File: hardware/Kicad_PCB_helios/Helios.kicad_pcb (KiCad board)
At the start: 2 copper layers, 75.2 x 61.1 mm, 101 parts, among them P1 USB_B, P2 CONN_01X25-SHIELD, U1 IP4220CZ6, U2 AP2114, U3 AN431B, U4 ISA_DC-DC_converter, U5 DAC084S085C, U6 TL084_v, U7 LM358, U8 TL084_v, U9 ATSAM4S, Y1 16MHz 18pF

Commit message: fix some outdated schematics
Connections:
- net /Amplifiers/+9V renamed /+9V
- net /Amplifiers/+B renamed /+B
- net /Amplifiers/+G renamed /+G
- net /Amplifiers/+Intensity renamed /+Int
- net /Amplifiers/+R renamed /+R
- net /Amplifiers/+X renamed /+X
- net /Amplifiers/+Y renamed /+Y
- net /Amplifiers/-9V renamed /-9V
- net /Amplifiers/-X renamed /-X
- net /Amplifiers/-Y renamed /-Y
- net /Amplifiers/2.5V renamed /2.5V
- net /Amplifiers/B renamed /B
- net /Amplifiers/G renamed /G
- net /Amplifiers/Intensity renamed /Int
- net /Amplifiers/R renamed /R
- net /Amplifiers/Shutter renamed /Shutter
- net /Amplifiers/Shutter_Out renamed /Shutter_Out
- net /Amplifiers/X renamed /X
- net /Amplifiers/Y renamed /Y
- net /DAC/!SYNC renamed /!SYNC
- net /DAC/Din renamed /MOSI
- net /DAC/SCLK renamed /SCLK
- net /Power Regulation/5V renamed /VCC
- C10 pad 1: /DAC/3.3V -> /3.3V
- C11 pad 1: /DAC/3.3V -> /3.3V
- C21 pad 1: /DAC/3.3V -> /3.3V
- C23 pad 1: /DAC/3.3V -> /3.3V
- C25 pad 1: /DAC/3.3V -> /3.3V
- C26 pad 1: /DAC/3.3V -> /3.3V
- C27 pad 1: /DAC/3.3V -> /3.3V
- ERASE pad 2: /DAC/3.3V -> (no net)
- R12 pad 1: /DAC/3.3V -> /3.3V
- R13 pad 1: /DAC/3.3V -> /3.3V
- U2 pad 2: /DAC/3.3V -> /3.3V
- U5 pad 1: /DAC/3.3V -> /3.3V
- U9 pad 18: /DAC/3.3V -> /3.3V
- U9 pad 45: /DAC/3.3V -> /3.3V
- U9 pad 58: /DAC/3.3V -> /3.3V
- U9 pad 7: /DAC/3.3V -> /3.3V
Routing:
- net /DAC/3.3V: track 95.3 -> 0.00 mm, vias 2 -> 0
- net /3.3V: track 0.00 -> 95.3 mm, vias 0 -> 2

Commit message: switch to new PSU on PCB. Fix bug in sdk example c++ app
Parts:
- removed REF** (x3): Fiducial_1mm_Dia_2.54mm_Outer_CopperTop, Fiducials:Fiducial_1mm_Dia_2.54mm_Outer_CopperTop
- added H1: MountingHole, MountingHole:MountingHole_2.7mm_M2.5, F.Cu at (161.0, 104.4)
- added H2: MountingHole, MountingHole:MountingHole_2.7mm_M2.5, F.Cu at (104.0, 156.4)
- added H3: MountingHole, MountingHole:MountingHole_2.7mm_M2.5, F.Cu at (104.0, 104.4)
- added H4: MountingHole, MountingHole:MountingHole_2.7mm_M2.5, F.Cu at (161.0, 156.4)
- U4: value ISA_DC-DC_converter -> ~; footprint personal:10-SMD-6 -> personal:CRV1DxxxxSC
- moved U4 11.5 mm to (128.7, 108.4), turned to 0 degrees
- moved C9 5.91 mm to (130.9, 117.8)
- moved C8 4.78 mm to (139.1, 117.8), turned to 180 degrees
- moved F1 0.35 mm to (112.2, 120.3)
- moved C3 0.20 mm to (114.7, 113.5)
- renumbered ERASE to ERASE1
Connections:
- C7 pad 1: Net-(C7-Pad1) -> Net-(U4-Vin)
- D1 pad 2: Net-(D1-Pad2) -> (no net)
- D2 pad 2: Net-(D2-Pad2) -> (no net)
- ERASE1 pad 2: (no net) -> /3.3V
- L2 pad 2: Net-(C7-Pad1) -> Net-(U4-Vin)
- P2 pad 12: (no net) -> /ProjReturn
- R14 pad 2: Net-(R14-Pad2) -> (no net)
- R15 pad 1: Net-(R14-Pad2) -> (no net)
- R16 pad 1: Net-(R16-Pad1) -> (no net)
- R17 pad 1: Net-(R17-Pad1) -> (no net)
- R18 pad 1: Net-(R18-Pad1) -> (no net)
- R19 pad 1: Net-(R19-Pad1) -> (no net)
- R20 pad 2: Net-(R18-Pad1) -> (no net)
- R21 pad 2: Net-(R19-Pad1) -> (no net)
- R22 pad 1: Net-(R22-Pad1) -> (no net)
- R24 pad 1: Net-(R24-Pad1) -> (no net)
- R25 pad 1: Net-(R25-Pad1) -> (no net)
- R26 pad 1: Net-(R26-Pad1) -> (no net)
- R27 pad 1: Net-(R27-Pad1) -> (no net)
- R28 pad 2: Net-(R26-Pad1) -> (no net)
- R29 pad 2: Net-(R27-Pad1) -> (no net)
- R30 pad 1: Net-(R30-Pad1) -> (no net)
- R31 pad 2: Net-(R31-Pad2) -> (no net)
- R32 pad 2: Net-(R31-Pad2) -> (no net)
- R33 pad 1: Net-(R33-Pad1) -> (no net)
- R34 pad 1: Net-(R34-Pad1) -> (no net)
- R35 pad 1: Net-(R35-Pad1) -> (no net)
- R36 pad 1: Net-(R36-Pad1) -> (no net)
- R37 pad 2: Net-(R35-Pad1) -> (no net)
- R38 pad 2: Net-(R36-Pad1) -> (no net)
- R39 pad 1: Net-(R39-Pad1) -> (no net)
- R40 pad 1: Net-(R40-Pad1) -> (no net)
- R41 pad 1: Net-(R41-Pad1) -> (no net)
- R42 pad 1: Net-(R42-Pad1) -> (no net)
- R43 pad 2: Net-(R39-Pad1) -> (no net)
- R44 pad 2: Net-(R40-Pad1) -> (no net)
- R45 pad 2: Net-(D1-Pad2) -> (no net)
- R46 pad 2: Net-(D1-Pad2) -> (no net)
- R47 pad 2: Net-(D2-Pad2) -> (no net)
- R48 pad 2: Net-(D2-Pad2) -> (no net)
- U1 pad 4: (no net) -> unconnected-(U1-IO3-Pad4)
- U1 pad 6: (no net) -> unconnected-(U1-IO4-Pad6)
- U4 pad 1: GND -> Net-(U4-Vin)
- U4 pad 2: Net-(C7-Pad1) -> GND
- U5 pad 8: /MOSI -> /DAC/Din
- U6 pad 10: Net-(R24-Pad1) -> (no net)
- U6 pad 12: Net-(R16-Pad1) -> (no net)
- U6 pad 13: Net-(R18-Pad1) -> (no net)
- U6 pad 2: Net-(R26-Pad1) -> (no net)
- U6 pad 3: Net-(R25-Pad1) -> (no net)
- U6 pad 5: Net-(R17-Pad1) -> (no net)
- U6 pad 6: Net-(R19-Pad1) -> (no net)
- U6 pad 9: Net-(R27-Pad1) -> (no net)
- U7 pad 1: Net-(R22-Pad1) -> (no net)
- U7 pad 2: Net-(R22-Pad1) -> (no net)
- U7 pad 3: Net-(R14-Pad2) -> (no net)
- U7 pad 5: Net-(R30-Pad1) -> (no net)
- U7 pad 6: Net-(R31-Pad2) -> (no net)
- U8 pad 10: Net-(R34-Pad1) -> (no net)
- U8 pad 12: Net-(R41-Pad1) -> (no net)
- U8 pad 13: Net-(R39-Pad1) -> (no net)
- U8 pad 2: Net-(R36-Pad1) -> (no net)
- U8 pad 3: Net-(R33-Pad1) -> (no net)
- U8 pad 5: Net-(R42-Pad1) -> (no net)
- U8 pad 6: Net-(R40-Pad1) -> (no net)
- U8 pad 9: Net-(R35-Pad1) -> (no net)
- U9 pad 39: (no net) -> /Microcontroller/NRST
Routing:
- net (no net): track 0.00 -> 141.3 mm, vias 0 -> 4
- net Net-(D1-Pad2): track 35.7 -> 0.00 mm
- net /+9V: track 67.6 -> 77.5 mm
- net Net-(D2-Pad2): track 9.74 -> 0.00 mm
- net GND: track 138.7 -> 129.4 mm
- net Net-(R35-Pad1): track 8.83 -> 0.00 mm
- net Net-(R39-Pad1): track 8.41 -> 0.00 mm, vias 2 -> 0
- net Net-(U4-Vin): track 0.00 -> 6.81 mm
- net /-9V: track 73.0 -> 66.4 mm
- net Net-(C7-Pad1): track 6.53 -> 0.00 mm
- net Net-(R24-Pad1): track 6.38 -> 0.00 mm
- net Net-(R17-Pad1): track 6.33 -> 0.00 mm
- net Net-(R34-Pad1): track 6.09 -> 0.00 mm
- net Net-(R18-Pad1): track 5.17 -> 0.00 mm, vias 2 -> 0
- net Net-(R40-Pad1): track 5.10 -> 0.00 mm
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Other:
- net class Default removed
- board text added: "Gitle Mikkelsen www.bitlasers.com gitlem@gmail.com"
- board text added: "Helios Laser DAC Rev 1.2"
- board text removed: "Gitle Mikkelsen Thomas L Heggland Bård Gustav Hole Eide"
- board text removed: "Helios Laser DAC Rev 1.1"
- board text removed: "gitlem@gmail.com"

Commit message: PCB 1.2
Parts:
- L1, L2, L3, R1, R10, R11, R12, R13, R14, R15, R16, R17, R18, R19, R2, R20, R21, R22, R23, R24, R25, R26, R27, R28, R29, R3, R30, R31, R32, R33, R34, R35, R36, R37, R38, R39, R4, R40, R41, R42, R43, R44, R45, R46, R47, R48, R5, R6, R7, R8, R9: footprint Resistors_SMD:R_0603 -> Resistor_SMD:R_0603_1608Metric
- moved Y1 0.18 mm to (115.7, 145.0)
- turned D1 to 90 degrees
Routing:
- net (no net): track 141.3 -> 143.0 mm

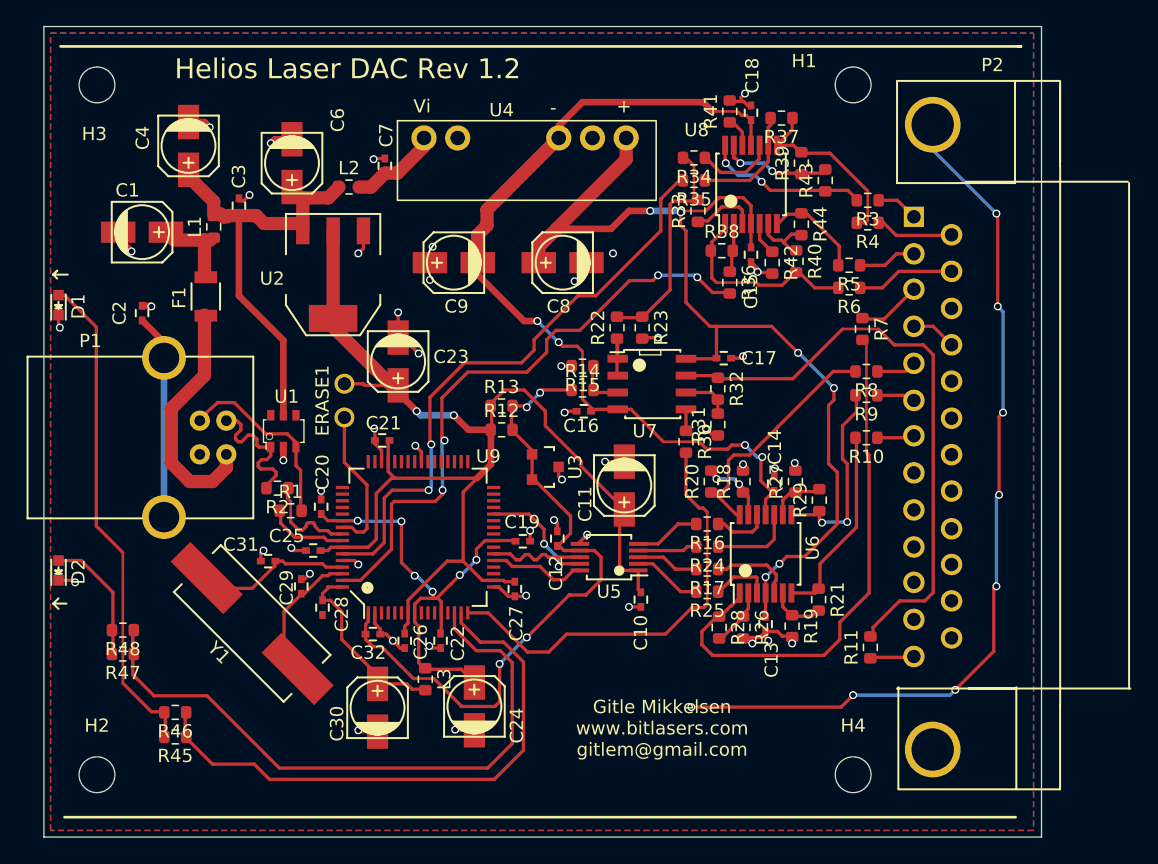
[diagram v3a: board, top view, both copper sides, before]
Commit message: Fix bug with D1 in pcb
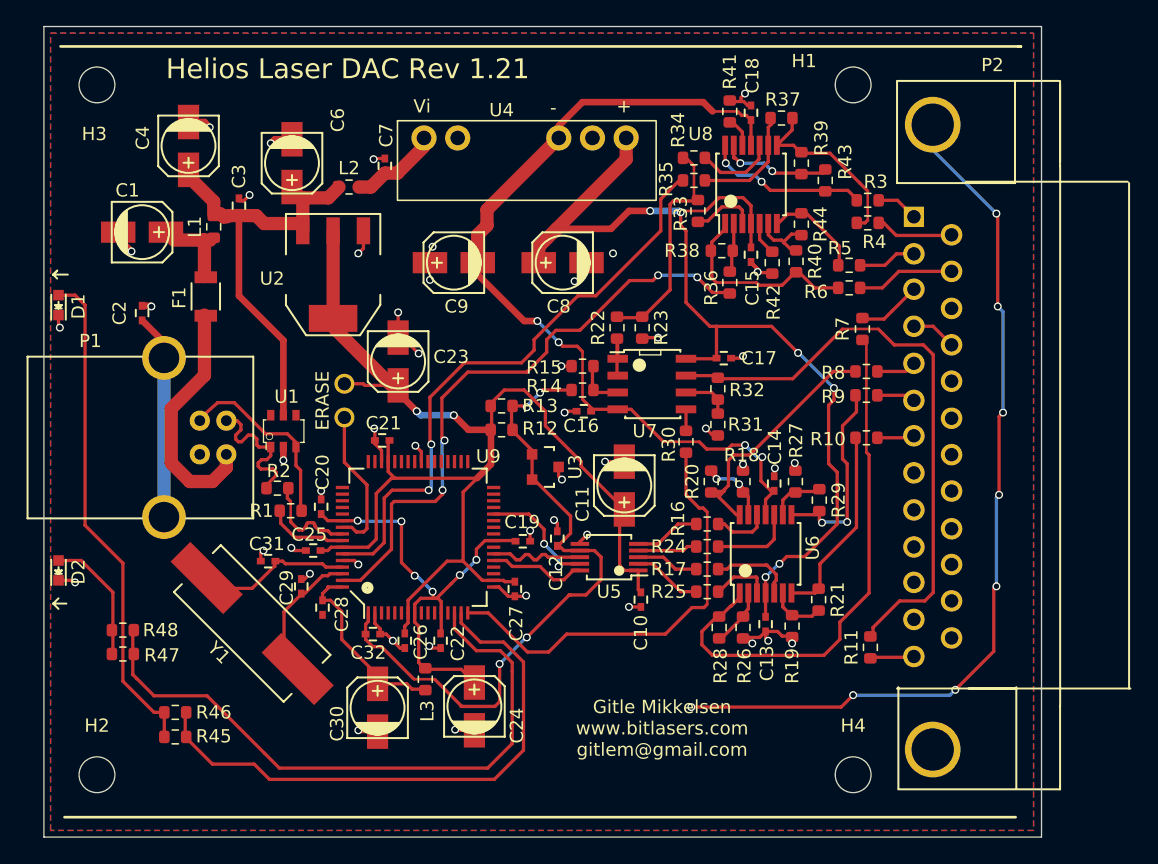
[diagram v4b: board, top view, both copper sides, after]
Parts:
- renumbered ERASE1 to ERASE
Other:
- board text added: "Helios Laser DAC Rev 1.21"
- board text removed: "Helios Laser DAC Rev 1.2"
